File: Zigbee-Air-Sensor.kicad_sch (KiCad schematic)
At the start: 14 parts, among them J1 USB_C_Receptacle_PowerOnly_6P, J2 Conn_01x04, J3 FH34SRJ-6S-0.5SH, J4 FH34SRJ-6S-0.5SH

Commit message: Add R24 Add testpoint for I2C Change CI image tag
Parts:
- added TP1, TP2, TP3, TP4: TestPoint, Zigbee-Air-Sensor:TestPoint_Pad_D0.6mm, symbol Connector:TestPoint
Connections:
- net BQ25628E/SCL: now also TP1.1
- net BQ25628E/SDA: now also TP2.1
- net ESP32-H2/IO26: now also TP3.1
- net ESP32-H2/IO27: now also TP4.1

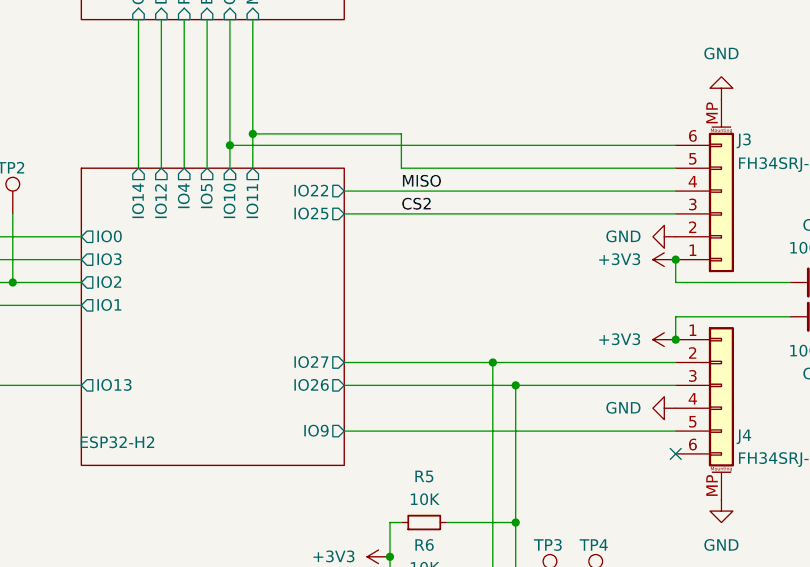
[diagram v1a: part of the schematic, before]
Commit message: Adjust slot size Change GPIO assignment
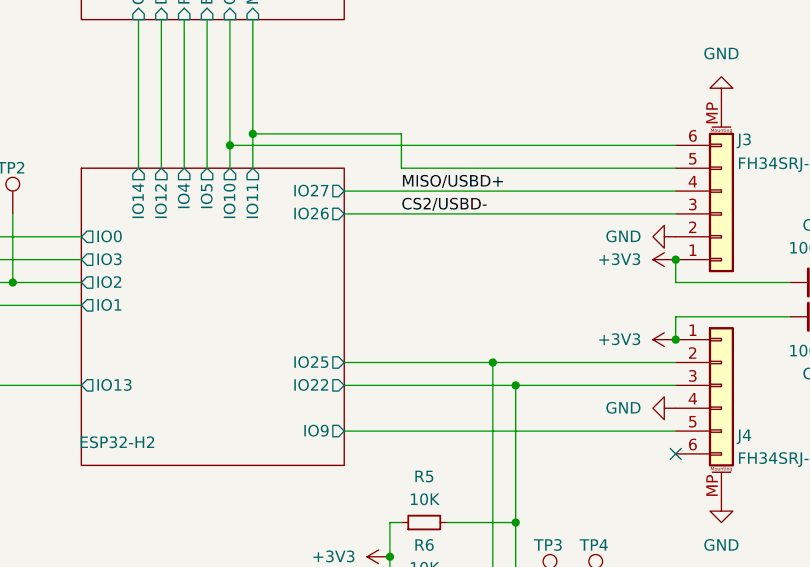
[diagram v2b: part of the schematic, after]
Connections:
- net CS2 renamed CS2/USBD-
- net ESP32-H2/IO26 renamed ESP32-H2/IO22
- net ESP32-H2/IO27 renamed ESP32-H2/IO25
- net MISO renamed MISO/USBD+
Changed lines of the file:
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@@
 	)
 	(junction
-		(at 198.12 101.6)
-		(diameter 0)
-		(color 0 0 0 0)
-	)
-	(junction
 		(at 218.44 99.06)
 		(diameter 0)
@@
 	)
 	(junction
-		(at 200.66 119.38)
+		(at 198.12 101.6)
 		(diameter 0)
 		(color 0 0 0 0)
 	)
 	(junction
-		(at 95.25 139.7)
+		(at 200.66 119.38)
 		(diameter 0)
 		(color 0 0 0 0)
 	)
 	(junction
-		(at 200.66 104.14)
+		(at 95.25 139.7)
 		(diameter 0)
 		(color 0 0 0 0)
@@
 	)
 	(junction
+		(at 200.66 104.14)
+		(diameter 0)
+		(color 0 0 0 0)
+	)
+	(junction
 		(at 109.22 90.17)
 		(diameter 0)
@@
 	(wire
 		(pts
-			(xy 101.6 52.07) (xy 111.76 52.07)
+			(xy 181.61 85.09) (xy 218.44 85.09)
 		)
 		(stroke
@@
 	(wire
 		(pts
-			(xy 64.77 118.11) (xy 72.39 118.11)
+			(xy 101.6 52.07) (xy 111.76 52.07)
 		)
 		(stroke
@@
 	(wire
 		(pts
-			(xy 200.66 119.38) (xy 200.66 130.81)
+			(xy 64.77 118.11) (xy 72.39 118.11)
 		)
 		(stroke
@@
 	(wire
 		(pts
-			(xy 181.61 101.6) (xy 198.12 101.6)
+			(xy 200.66 119.38) (xy 200.66 130.81)
 		)
 		(stroke
@@
 	(wire
 		(pts
+			(xy 181.61 82.55) (xy 218.44 82.55)
+		)
+		(stroke
+			(width 0)
+			(type default)
+		)
+	)
+	(wire
+		(pts
 			(xy 69.85 55.88) (xy 69.85 83.82)
 		)
@@
 	(wire
 		(pts
-			(xy 181.61 104.14) (xy 200.66 104.14)
-		)
-		(stroke
-			(width 0)
-			(type default)
-		)
-	)
-	(wire
-		(pts
 			(xy 101.6 57.15) (xy 114.3 57.15)
 		)
@@
 	(wire
 		(pts
+			(xy 181.61 104.14) (xy 200.66 104.14)
+		)
+		(stroke
+			(width 0)
+			(type default)
+		)
+	)
+	(wire
+		(pts
 			(xy 102.87 147.32) (xy 114.3 147.32)
 		)
@@
 	(wire
 		(pts
-			(xy 219.71 133.35) (xy 209.55 133.35)
+			(xy 181.61 101.6) (xy 198.12 101.6)
 		)
 		(stroke
@@
 	(wire
 		(pts
-			(xy 218.44 99.06) (xy 218.44 96.52)
+			(xy 219.71 133.35) (xy 209.55 133.35)
 		)
 		(stroke
@@
 	(wire
 		(pts
-			(xy 204.47 130.81) (xy 219.71 130.81)
+			(xy 218.44 99.06) (xy 218.44 96.52)
 		)
 		(stroke
@@
 	(wire
 		(pts
-			(xy 168.91 77.47) (xy 168.91 80.01)
+			(xy 204.47 130.81) (xy 219.71 130.81)
 		)
 		(stroke
@@
 	(wire
 		(pts
-			(xy 114.3 104.14) (xy 152.4 104.14)
+			(xy 168.91 77.47) (xy 168.91 80.01)
 		)
 		(stroke
@@
 	(wire
 		(pts
-			(xy 181.61 85.09) (xy 218.44 85.09)
+			(xy 114.3 104.14) (xy 152.4 104.14)
 		)
 		(stroke
@@
 	(wire
 		(pts
-			(xy 181.61 82.55) (xy 218.44 82.55)
-		)
-		(stroke
-			(width 0)
-			(type default)
-		)
-	)
-	(wire
-		(pts
 			(xy 236.22 92.71) (xy 242.57 92.71)
 		)
@@
 		)
 	)
-	(label "CS2"
-		(at 187.96 85.09 0)
+	(label "MISO{slash}USBD+"
+		(at 187.96 82.55 0)
 		(fields_autoplaced yes)
 		(effects
@@
 		)
 	)
-	(label "MISO"
-		(at 187.96 82.55 0)
+	(label "CS2{slash}USBD-"
+		(at 187.96 85.09 0)
 		(fields_autoplaced yes)
 		(effects
@@
 			)
 		)
-		(pin "IO25" output
+		(pin "IO26" output
 			(at 181.61 85.09 0)
 			(effects
@@
 			)
 		)
-		(pin "IO22" output
+		(pin "IO27" output
 			(at 181.61 82.55 0)
 			(effects
@@
 			)
 		)
-		(pin "IO26" output
-			(at 181.61 104.14 0)
+		(pin "IO3" output
+			(at 152.4 90.17 180)
 			(effects
 				(font
 					(size 1.27 1.27)
 				)
-				(justify right)
+				(justify left)
 			)
 		)
-		(pin "IO27" output
-			(at 181.61 101.6 0)
+		(pin "IO2" output
+			(at 152.4 92.71 180)
 			(effects
 				(font
 					(size 1.27 1.27)
 				)
-				(justify right)
+				(justify left)
 			)
 		)
-		(pin "IO3" output
-			(at 152.4 90.17 180)
+		(pin "IO9" output
+			(at 181.61 109.22 0)
 			(effects
 				(font
 					(size 1.27 1.27)
 				)
-				(justify left)
+				(justify right)
 			)
 		)
-		(pin "IO2" output
-			(at 152.4 92.71 180)
+		(pin "IO13" output
+			(at 152.4 104.14 180)
 			(effects
 				(font
@@
 			)
 		)
-		(pin "IO9" output
-			(at 181.61 109.22 0)
+		(pin "IO22" output
+			(at 181.61 104.14 0)
 			(effects
 				(font
@@
 			)
 		)
-		(pin "IO13" output
-			(at 152.4 104.14 180)
+		(pin "IO25" output
+			(at 181.61 101.6 0)
 			(effects
 				(font
 					(size 1.27 1.27)
 				)
-				(justify left)
+				(justify right)
 			)
 		)
